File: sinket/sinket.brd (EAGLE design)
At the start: 30 x 30 mm, 8 parts, among them IC1 TINY13-20PU

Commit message: replace uC with new ATtiny25 device package symbol
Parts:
- IC1: value TINY13-20PU -> ATTINY25-20PU; device atmel:DIL08 -> n39_avr:8P3
- turned IC1 to 90 degrees
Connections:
- net +5V: now also IC1.8
- net VBUS: no longer IC1.8
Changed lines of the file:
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@@
 <element name="JP1" library="pinhead" package="1X05" value="" x="15" y="25.16" locked="yes"/>
 <element name="JP2" library="pinhead" package="1X05" value="" x="15" y="4.84" locked="yes"/>
-<element name="IC1" library="atmel" package="DIL08" value="TINY13-20PU" x="20.32" y="15.24" rot="MR180">
-<attribute name="OC_NEWARK" value="96K6521" x="20.32" y="15.24" size="1.778" layer="28" rot="MR180" display="off"/>
-<attribute name="MPN" value="ATTINY13-20PU" x="20.32" y="15.24" size="1.778" layer="28" rot="MR180" display="off"/>
-<attribute name="MF" value="" x="20.32" y="15.24" size="1.778" layer="28" rot="MR180" display="off"/>
-<attribute name="OC_FARNELL" value="9171550" x="20.32" y="15.24" size="1.778" layer="28" rot="MR180" display="off"/>
+<element name="IC1" library="n39_avr" package="8P3" value="ATTINY25-20PU" x="20.32" y="15.24" rot="MR90">
+<attribute name="REICHELT" value="ATTINY 25-20 PU" x="20.32" y="15.24" size="1.778" layer="28" rot="MR90" display="off"/>
 </element>
 <element name="U$2" library="holes" package="3,2-PAD" value="" x="4" y="4"/>
@@
 </elements>
 <signals>
-<signal name="+5V">
+<signal name="+5V" class="1">
 <contactref element="JP2" pad="5"/>
+<contactref element="IC1" pad="8"/>
+<wire x1="20.08" y1="4.84" x2="24.13" y2="11.43" width="0" layer="19" extent="1-1"/>
 </signal>
-<signal name="VBUS">
+<signal name="VBUS" class="1">
 <contactref element="U$1" pad="1"/>
-<contactref element="IC1" pad="8"/>
 <contactref element="JP2" pad="1"/>
-<wire x1="8.55" y1="13.4" x2="16.51" y2="11.43" width="0" layer="19" extent="16-16"/>
 <wire x1="9.92" y1="4.84" x2="8.55" y2="13.4" width="0" layer="19" extent="16-16"/>
 </signal>
-<signal name="GND">
+<signal name="GND" class="1">
 <contactref element="U$1" pad="5"/>
 <contactref element="JP1" pad="2"/>
-<contactref element="IC1" pad="4"/>
 <polygon width="0.4064" layer="16">
 <vertex x="4" y="0"/>
@@
 <vertex x="0" y="4" curve="90"/>
 </polygon>
+<contactref element="IC1" pad="4"/>
 </signal>
-<signal name="VBAT">
+<signal name="VBAT" class="1">
 <contactref element="JP1" pad="1"/>
 </signal>

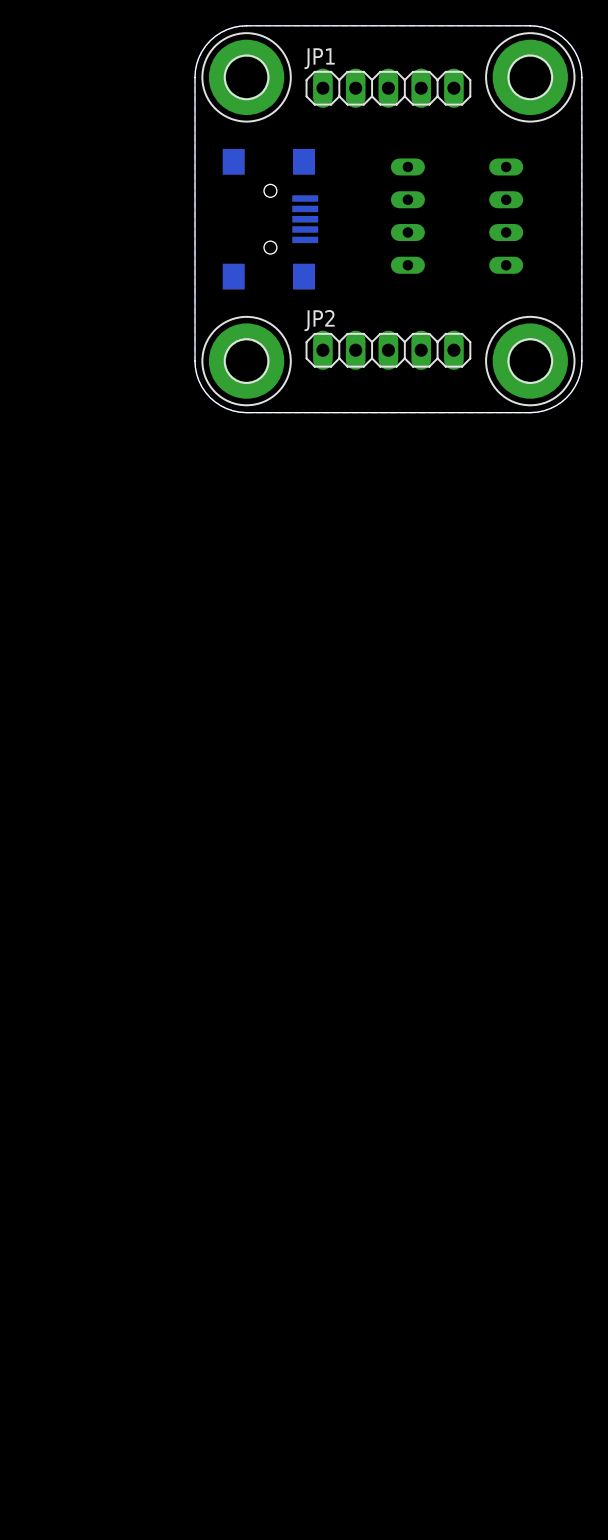
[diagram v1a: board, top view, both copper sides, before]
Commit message: proceed schematics (stopped because a schottky diode is missing)
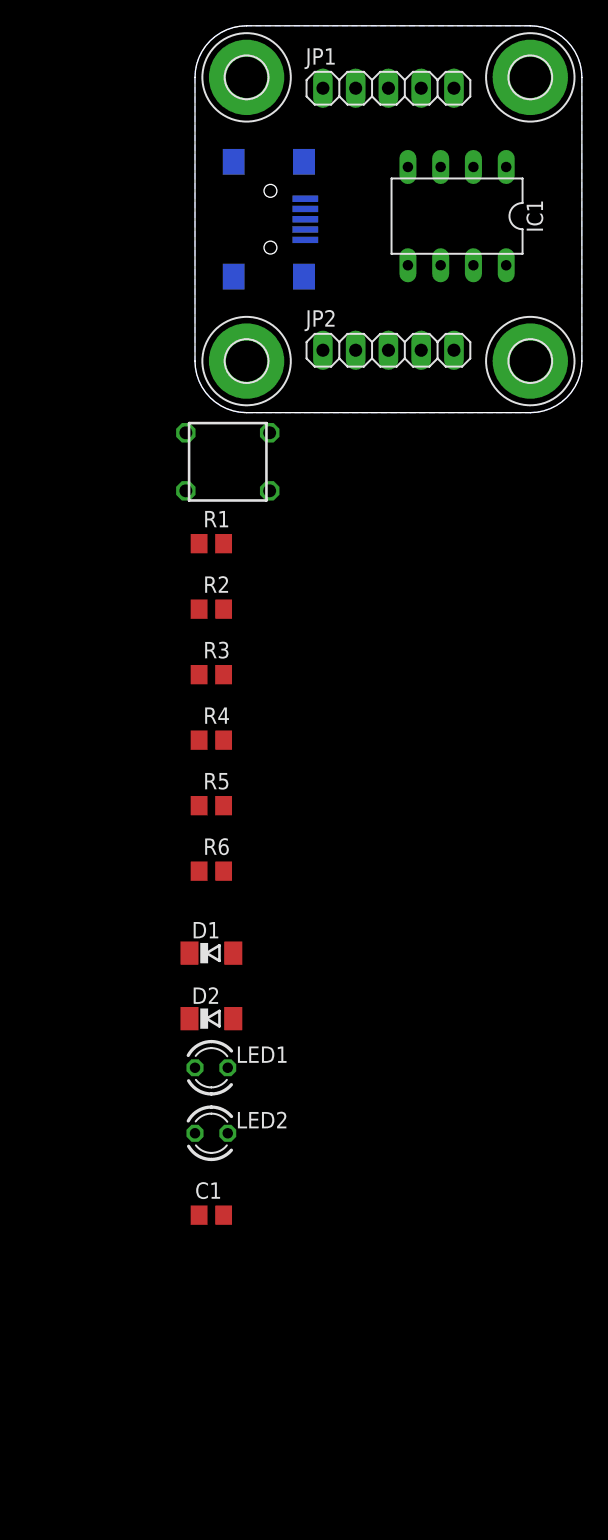
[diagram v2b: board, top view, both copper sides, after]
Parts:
- added C1: 100n, rcl:C0805
- added D1, D2: 3V6, diode:SOD80C
- added LED1: red, led:LED3MM
- added LED2: green, led:LED3MM
- added R1: 10k, rcl:R0805
- added R2, R5, R6: 1k5, rcl:R0805
- added R3, R4: 68, rcl:R0805
- added U$6: JTP-1130C, n39:JTP-1130
- IC1: value ATTINY25-20PU -> ATTINY85-20PU
- flipped IC1 to the top, turned to 180 degrees
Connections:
- new net !RESET: IC1.1, JP1.5, R1.1, U$6.3, U$6.4
- new net B0: IC1.5, JP2.2
- new net B1: IC1.6, JP2.3, R2.1
- new net B2: IC1.7, JP2.4
- new net B3: IC1.2, JP1.4, R3.1
- new net B4: IC1.3, JP1.3, R4.1
- new net N$1: D1.C, R3.2, R6.2, U$1.2
- new net N$3: D2.C, R4.2, U$1.3
- new net N$4: LED1.A, R2.2
- new net N$5: LED2.A, R5.2
- net +5V: now also C1.1, R1.2, R5.1, R6.1
- net GND: now also C1.2, D1.A, D2.A, LED1.K, LED2.K, U$6.1, U$6.2
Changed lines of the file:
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@@
 <element name="JP1" library="pinhead" package="1X05" value="" x="15" y="25.16" locked="yes"/>
 <element name="JP2" library="pinhead" package="1X05" value="" x="15" y="4.84" locked="yes"/>
-<element name="IC1" library="n39_avr" package="8P3" value="ATTINY25-20PU" x="20.32" y="15.24" rot="MR90">
-<attribute name="REICHELT" value="ATTINY 25-20 PU" x="20.32" y="15.24" size="1.778" layer="28" rot="MR90" display="off"/>
+<element name="IC1" library="n39_avr" package="8P3" value="ATTINY85-20PU" x="20.32" y="15.24" rot="R180">
+<attribute name="REICHELT" value="ATTINY 25-20 PU" x="20.32" y="15.24" size="1.778" layer="27" rot="R180" display="off"/>
 </element>
 <element name="U$2" library="holes" package="3,2-PAD" value="" x="4" y="4"/>
@@
 <element name="U$4" library="holes" package="3,2-PAD" value="" x="26" y="26"/>
 <element name="U$5" library="holes" package="3,2-PAD" value="" x="4" y="26"/>
+<element name="U$6" library="n39" package="JTP-1130" value="JTP-1130C" x="2.54" y="-3.81">
+<attribute name="REICHELT" value="TASTER 9305" x="2.54" y="-3.81" size="1.778" layer="27" display="off"/>
+</element>
+<element name="R1" library="rcl" package="R0805" value="10k" x="1.27" y="-10.16"/>
+<element name="R2" library="rcl" package="R0805" value="1k5" x="1.27" y="-15.24"/>
+<element name="R3" library="rcl" package="R0805" value="68" x="1.27" y="-20.32"/>
+<element name="R4" library="rcl" package="R0805" value="68" x="1.27" y="-25.4"/>
+<element name="R5" library="rcl" package="R0805" value="1k5" x="1.27" y="-30.48"/>
+<element name="R6" library="rcl" package="R0805" value="1k5" x="1.27" y="-35.56"/>
+<element name="D1" library="diode" package="SOD80C" value="3V6" x="1.27" y="-41.91"/>
+<element name="D2" library="diode" package="SOD80C" value="3V6" x="1.27" y="-46.99"/>
+<element name="LED1" library="led" package="LED3MM" value="red" x="1.27" y="-50.8"/>
+<element name="LED2" library="led" package="LED3MM" value="green" x="1.27" y="-55.88"/>
+<element name="C1" library="rcl" package="C0805" value="100n" x="1.27" y="-62.23"/>
 </elements>
 <signals>
@@
 <contactref element="JP2" pad="5"/>
 <contactref element="IC1" pad="8"/>
-<wire x1="20.08" y1="4.84" x2="24.13" y2="11.43" width="0" layer="19" extent="1-1"/>
+<contactref element="R6" pad="1"/>
+<contactref element="R1" pad="2"/>
+<contactref element="R5" pad="1"/>
+<contactref element="C1" pad="1"/>
+<wire x1="0.32" y1="-35.56" x2="0.32" y2="-62.23" width="0" layer="19" extent="1-1"/>
+<wire x1="0.32" y1="-30.48" x2="0.32" y2="-35.56" width="0" layer="19" extent="1-1"/>
+<wire x1="2.22" y1="-10.16" x2="0.32" y2="-30.48" width="0" layer="19" extent="1-1"/>
+<wire x1="20.08" y1="4.84" x2="2.22" y2="-10.16" width="0" layer="19" extent="1-1"/>
+<wire x1="24.13" y1="11.43" x2="20.08" y2="4.84" width="0" layer="19" extent="1-1"/>
 </signal>
 <signal name="VBUS" class="1">
@@
 </polygon>
 <contactref element="IC1" pad="4"/>
+<contactref element="D2" pad="A"/>
+<contactref element="D1" pad="A"/>
+<contactref element="U$6" pad="1"/>
+<contactref element="U$6" pad="2"/>
+<contactref element="LED1" pad="K"/>
+<contactref element="LED2" pad="K"/>
+<contactref element="C1" pad="2"/>
+<wire x1="2.54" y1="-55.88" x2="2.22" y2="-62.23" width="0" layer="19" extent="1-1"/>
+<wire x1="2.54" y1="-50.8" x2="2.54" y2="-55.88" width="0" layer="19" extent="1-1"/>
+<wire x1="2.97" y1="-46.99" x2="2.54" y2="-50.8" width="0" layer="19" extent="1-1"/>
+<wire x1="2.97" y1="-41.91" x2="2.97" y2="-46.99" width="0" layer="19" extent="1-1"/>
+<wire x1="5.79" y1="-6.06" x2="2.97" y2="-41.91" width="0" layer="19" extent="1-1"/>
+<wire x1="-0.71" y1="-6.06" x2="5.79" y2="-6.06" width="0" layer="19" extent="1-1"/>
+<wire x1="8.55" y1="16.6" x2="5.79" y2="-6.06" width="0" layer="19" extent="16-16"/>
+<wire x1="16.51" y1="19.05" x2="8.55" y2="16.6" width="0" layer="19" extent="16-16"/>
+<wire x1="12.46" y1="25.16" x2="16.51" y2="19.05" width="0" layer="19" extent="1-1"/>
 </signal>
 <signal name="VBAT" class="1">
 <contactref element="JP1" pad="1"/>
 </signal>
+<signal name="N$1">
+<contactref element="U$1" pad="2"/>
+<contactref element="R3" pad="2"/>
+<contactref element="R6" pad="2"/>
+<contactref element="D1" pad="C"/>
+<wire x1="2.22" y1="-35.56" x2="-0.43" y2="-41.91" width="0" layer="19" extent="1-1"/>
+<wire x1="2.22" y1="-20.32" x2="2.22" y2="-35.56" width="0" layer="19" extent="1-1"/>
+<wire x1="8.55" y1="14.2" x2="2.22" y2="-20.32" width="0" layer="19" extent="1-16"/>
+</signal>
+<signal name="B3">
+<contactref element="R3" pad="1"/>
+<contactref element="IC1" pad="2"/>
+<contactref element="JP1" pad="4"/>
+<wire x1="21.59" y1="19.05" x2="17.54" y2="25.16" width="0" layer="19" extent="1-1"/>
+<wire x1="0.32" y1="-20.32" x2="21.59" y2="19.05" width="0" layer="19" extent="1-1"/>
+</signal>
+<signal name="N$3">
+<contactref element="U$1" pad="3"/>
+<contactref element="R4" pad="2"/>
+<contactref element="D2" pad="C"/>
+<wire x1="2.22" y1="-25.4" x2="-0.43" y2="-46.99" width="0" layer="19" extent="1-1"/>
+<wire x1="8.55" y1="15" x2="2.22" y2="-25.4" width="0" layer="19" extent="1-16"/>
+</signal>
+<signal name="B4">
+<contactref element="R4" pad="1"/>
+<contactref element="IC1" pad="3"/>
+<contactref element="JP1" pad="3"/>
+<wire x1="19.05" y1="19.05" x2="15" y2="25.16" width="0" layer="19" extent="1-1"/>
+<wire x1="0.32" y1="-25.4" x2="19.05" y2="19.05" width="0" layer="19" extent="1-1"/>
+</signal>
+<signal name="!RESET">
+<contactref element="IC1" pad="1"/>
+<contactref element="U$6" pad="4"/>
+<contactref element="R1" pad="1"/>
+<contactref element="U$6" pad="3"/>
+<contactref element="JP1" pad="5"/>
+<wire x1="24.13" y1="19.05" x2="20.08" y2="25.16" width="0" layer="19" extent="1-1"/>
+<wire x1="5.79" y1="-1.56" x2="24.13" y2="19.05" width="0" layer="19" extent="1-1"/>
+<wire x1="-0.71" y1="-1.56" x2="5.79" y2="-1.56" width="0" layer="19" extent="1-1"/>
+<wire x1="0.32" y1="-10.16" x2="-0.71" y2="-1.56" width="0" layer="19" extent="1-1"/>
+</signal>
+<signal name="B1">
+<contactref element="IC1" pad="6"/>
+<contactref element="R2" pad="1"/>
+<contactref element="JP2" pad="3"/>
+<wire x1="15" y1="4.84" x2="19.05" y2="11.43" width="0" layer="19" extent="1-1"/>
+<wire x1="0.32" y1="-15.24" x2="15" y2="4.84" width="0" layer="19" extent="1-1"/>
+</signal>
+<signal name="N$4">
+<contactref element="R2" pad="2"/>
+<contactref element="LED1" pad="A"/>
+<wire x1="2.22" y1="-15.24" x2="0" y2="-50.8" width="0" layer="19" extent="1-1"/>
+</signal>
+<signal name="N$5">
+<contactref element="LED2" pad="A"/>
+<contactref element="R5" pad="2"/>
+<wire x1="2.22" y1="-30.48" x2="0" y2="-55.88" width="0" layer="19" extent="1-1"/>
+</signal>
+<signal name="B0">
+<contactref element="IC1" pad="5"/>
+<contactref element="JP2" pad="2"/>
+<wire x1="12.46" y1="4.84" x2="16.51" y2="11.43" width="0" layer="19" extent="1-1"/>
+</signal>
+<signal name="B2">
+<contactref element="IC1" pad="7"/>
+<contactref element="JP2" pad="4"/>
+<wire x1="17.54" y1="4.84" x2="21.59" y2="11.43" width="0" layer="19" extent="1-1"/>
+</signal>
 </signals>

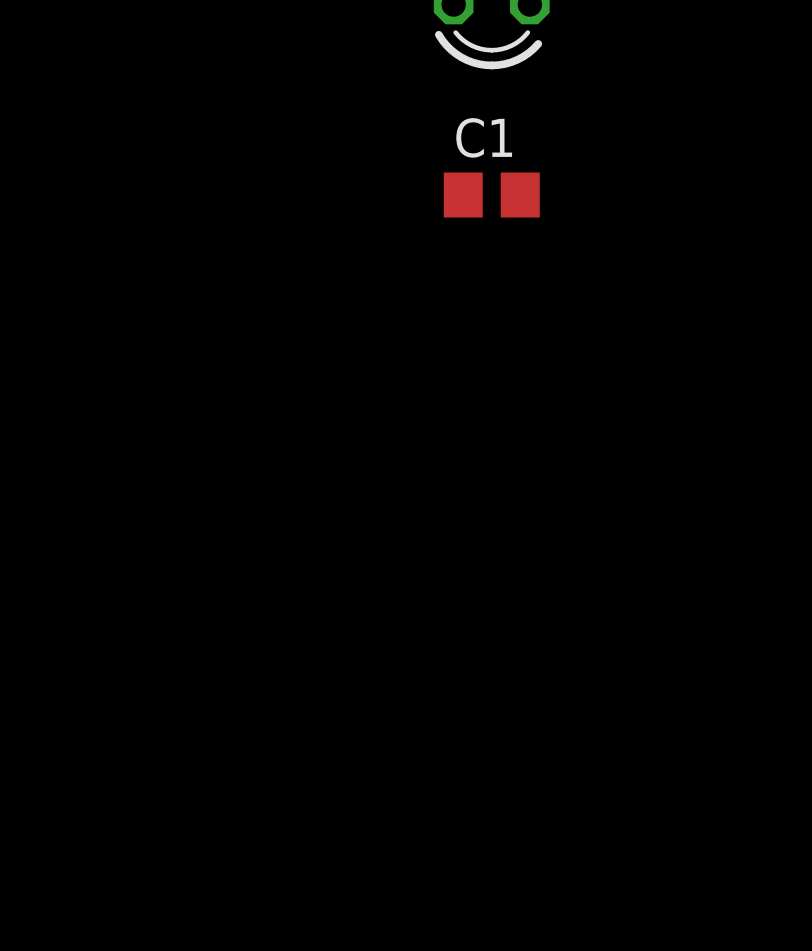
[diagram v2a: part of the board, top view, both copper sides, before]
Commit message: add remaining parts to schematic
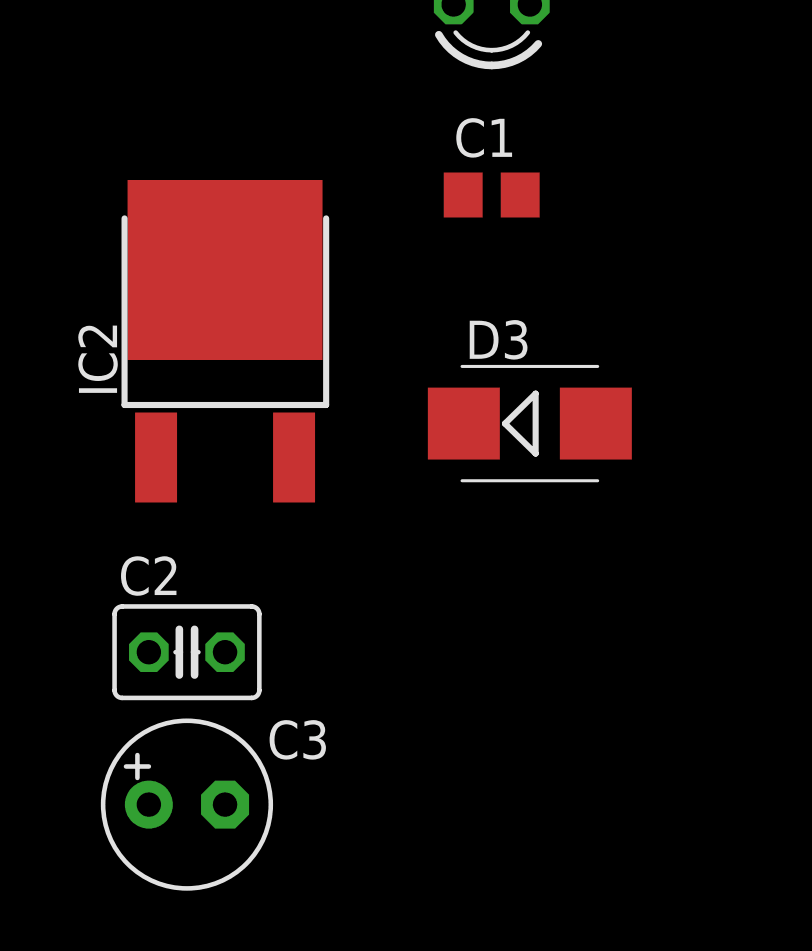
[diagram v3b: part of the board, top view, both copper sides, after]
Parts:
- added C2: 470n, rcl:C025-030X050
- added C3: 47u, rcl:E2,5-6
- added D3: MBRS240LT3, diode:SMB
- added IC2: TS2940CP50S, n39:TO-252
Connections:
- net +5V: now also C3.+, D3.C, IC2.3
- net GND: now also C2.2, C3.-, IC2.2
- net VBAT: now also C2.1, IC2.1
- net VBUS: now also D3.A
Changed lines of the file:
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@@
 <element name="LED2" library="led" package="LED3MM" value="green" x="1.27" y="-55.88"/>
 <element name="C1" library="rcl" package="C0805" value="100n" x="1.27" y="-62.23"/>
+<element name="D3" library="diode" package="SMB" value="MBRS240LT3" x="2.54" y="-69.85"/>
+<element name="IC2" library="n39" package="TO-252" value="TS2940CP50S" x="-7.62" y="-68.58">
+<attribute name="REICHELT" value="TS 2940 CP50" x="-7.62" y="-68.58" size="1.778" layer="27" display="off"/>
+</element>
+<element name="C2" library="rcl" package="C025-030X050" value="470n" x="-8.89" y="-77.47"/>
+<element name="C3" library="rcl" package="E2,5-6" value="47u" x="-8.89" y="-82.55"/>
 </elements>
 <signals>
@@
 <contactref element="R5" pad="1"/>
 <contactref element="C1" pad="1"/>
+<contactref element="D3" pad="C"/>
+<contactref element="IC2" pad="3"/>
+<contactref element="C3" pad="+"/>
+<wire x1="-5.32" y1="-70.98" x2="-10.16" y2="-82.55" width="0" layer="19" extent="1-1"/>
+<wire x1="0.34" y1="-69.85" x2="-5.32" y2="-70.98" width="0" layer="19" extent="1-1"/>
+<wire x1="0.32" y1="-62.23" x2="0.34" y2="-69.85" width="0" layer="19" extent="1-1"/>
 <wire x1="0.32" y1="-35.56" x2="0.32" y2="-62.23" width="0" layer="19" extent="1-1"/>
 <wire x1="0.32" y1="-30.48" x2="0.32" y2="-35.56" width="0" layer="19" extent="1-1"/>
@@
 <contactref element="U$1" pad="1"/>
 <contactref element="JP2" pad="1"/>
-<wire x1="9.92" y1="4.84" x2="8.55" y2="13.4" width="0" layer="19" extent="16-16"/>
+<contactref element="D3" pad="A"/>
+<wire x1="9.92" y1="4.84" x2="4.74" y2="-69.85" width="0" layer="19" extent="1-1"/>
+<wire x1="8.55" y1="13.4" x2="9.92" y2="4.84" width="0" layer="19" extent="16-16"/>
 </signal>
 <signal name="GND" class="1">
@@
 <contactref element="LED2" pad="K"/>
 <contactref element="C1" pad="2"/>
+<contactref element="IC2" pad="2"/>
+<contactref element="C2" pad="2"/>
+<contactref element="C3" pad="-"/>
+<contactref element="IC2" pad="2"/>
+<wire x1="-7.62" y1="-77.47" x2="-7.62" y2="-82.55" width="0" layer="19" extent="1-1"/>
+<wire x1="-7.62" y1="-64.73" x2="-7.62" y2="-77.47" width="0" layer="19" extent="1-1"/>
+<wire x1="2.22" y1="-62.23" x2="-7.62" y2="-64.73" width="0" layer="19" extent="1-1"/>
 <wire x1="2.54" y1="-55.88" x2="2.22" y2="-62.23" width="0" layer="19" extent="1-1"/>
 <wire x1="2.54" y1="-50.8" x2="2.54" y2="-55.88" width="0" layer="19" extent="1-1"/>
@@
 <signal name="VBAT" class="1">
 <contactref element="JP1" pad="1"/>
+<contactref element="IC2" pad="1"/>
+<contactref element="C2" pad="1"/>
+<wire x1="-9.92" y1="-70.98" x2="-10.16" y2="-77.47" width="0" layer="19" extent="1-1"/>
+<wire x1="9.92" y1="25.16" x2="-9.92" y2="-70.98" width="0" layer="19" extent="1-1"/>
 </signal>
 <signal name="N$1">
